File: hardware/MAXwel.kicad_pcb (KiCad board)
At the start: 2 copper layers, 85.1 x 87.2 mm, 155 parts, among them J1 Conn_02x05_Odd_Even, J2 Conn_02x12_Counter_Clockwise, J3 Barrel_Jack_Switch_Pin3Ring, SW1 SW_Push_Dual, SW10 SW_Wuerth_450301014042, SW11 SW_Wuerth_450301014042, SW12 SW_Wuerth_450301014042, SW13 SW_Wuerth_450301014042, SW2 SW_Push_Dual, SW3 SW_Push_Dual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

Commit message: first successfull redesign
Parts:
- moved R1 12.0 mm to (130.6, 58.7)
- moved D1 12.0 mm to (126.5, 58.7)
- moved C1 12.0 mm to (143.3, 47.5), turned to 180 degrees
- moved C2 11.1 mm to (152.3, 48.8), turned to -90 degrees
- moved C5 9.46 mm to (143.3, 46.0), turned to 180 degrees
- moved R31 6.24 mm to (117.9, 94.5), turned to 0 degrees
- moved X2 5.70 mm to (143.3, 51.3), turned to -90 degrees
- moved R45 4.45 mm to (122.2, 63.0), turned to 90 degrees
- moved R50 4.28 mm to (122.2, 33.5), turned to 90 degrees
- moved R42 4.23 mm to (122.2, 77.7), turned to 90 degrees
- moved R48 4.14 mm to (122.2, 48.3), turned to 90 degrees
- moved R49 3.54 mm to (122.2, 44.7), turned to -90 degrees
- moved R43 3.42 mm to (122.2, 74.2), turned to -90 degrees
- moved R51 3.39 mm to (122.2, 30.0), turned to -90 degrees
- moved R33 3.30 mm to (118.1, 84.3), turned to 135 degrees
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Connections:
- C13 pad 1: Net-(C13-Pad1) -> Net-(U5-IO1_4)
- C14 pad 1: Net-(C14-Pad1) -> Net-(U5-IO1_3)
- C3 pad 1: Net-(C3-Pad1) -> Net-(U5-IO1_20)
- C9 pad 1: Net-(C9-Pad1) -> Net-(U5-IO1_19)
- D7 pad 2: unconnected-(D7-A-Pad2) -> Net-(D7-A)
- R1 pad 1: unconnected-(R1-Pad1) -> Net-(U5-IO1_15)
- R2 pad 1: unconnected-(R2-Pad1) -> Net-(U5-IO1_5)
- R3 pad 1: unconnected-(R3-Pad1) -> Net-(U5-IO1_6)
- R4 pad 1: unconnected-(R4-Pad1) -> Net-(U5-IO1_7)
- R42 pad 1: Net-(C3-Pad1) -> Net-(U5-IO1_20)
- R45 pad 1: Net-(C9-Pad1) -> Net-(U5-IO1_19)
- R48 pad 1: Net-(C13-Pad1) -> Net-(U5-IO1_4)
- R5 pad 1: unconnected-(R5-Pad1) -> Net-(U5-IO1_8)
- R50 pad 1: Net-(C14-Pad1) -> Net-(U5-IO1_3)
- R53 pad 2: unconnected-(R53-Pad2) -> Net-(D7-A)
- R62 pad 1: unconnected-(R62-Pad1) -> Net-(U5-IO1_16)
- R63 pad 1: unconnected-(R63-Pad1) -> Net-(U5-IO1_17)
- R65 pad 1: unconnected-(R65-Pad1) -> Net-(U5-IO1_18)
- U5 pad 15: unconnected-(U5-IO1_15-Pad15) -> Net-(U5-IO1_15)
- U5 pad 16: unconnected-(U5-IO1_16-Pad16) -> Net-(U5-IO1_16)
- U5 pad 17: unconnected-(U5-IO1_17-Pad17) -> Net-(U5-IO1_17)
- U5 pad 18: unconnected-(U5-IO1_18-Pad18) -> Net-(U5-IO1_18)
- U5 pad 19: unconnected-(U5-IO1_19-Pad19) -> Net-(U5-IO1_19)
- U5 pad 20: unconnected-(U5-IO1_20-Pad20) -> Net-(U5-IO1_20)
- U5 pad 3: unconnected-(U5-IO1_3-Pad3) -> Net-(U5-IO1_3)
- U5 pad 4: unconnected-(U5-IO1_4-Pad4) -> Net-(U5-IO1_4)
- U5 pad 5: unconnected-(U5-IO1_5-Pad5) -> Net-(U5-IO1_5)
- U5 pad 6: unconnected-(U5-IO1_6-Pad6) -> Net-(U5-IO1_6)
- U5 pad 7: unconnected-(U5-IO1_7-Pad7) -> Net-(U5-IO1_7)
- U5 pad 8: unconnected-(U5-IO1_8-Pad8) -> Net-(U5-IO1_8)
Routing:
- net +3V3: track 0.00 -> 371.0 mm, vias 0 -> 8
- net Net-(J1-Pin_5): track 0.00 -> 82.3 mm
- net Net-(J1-Pin_9): track 0.00 -> 76.5 mm
- net Net-(U5-IO1_3): track 0.00 -> 57.0 mm
- net Net-(J1-Pin_3): track 0.00 -> 55.8 mm
- net Net-(J1-Pin_1): track 0.00 -> 54.7 mm
- net Net-(U5-IO1_4): track 0.00 -> 54.5 mm
- net Net-(U5-IO1_20): track 0.00 -> 48.1 mm
- net Net-(U5-IO1_19): track 0.00 -> 46.8 mm
- net Net-(U5-IO1_8): track 0.00 -> 41.4 mm
- net Net-(U5-IO1_7): track 0.00 -> 39.7 mm
- net Net-(U5-IO1_6): track 0.00 -> 38.0 mm
- net Net-(U5-IO1_5): track 0.00 -> 36.3 mm
- net GND: track 30.1 -> 65.5 mm, vias 0 -> 25
- net Net-(U5-IO1_15): track 0.00 -> 28.3 mm
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- added copper zone on B.Cu, net +3V3

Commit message: squashing pcb layout
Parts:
- moved R77 13.7 mm to (174.2, 70.9), turned to 90 degrees
- moved D17 6.80 mm to (176.3, 74.2), turned to -90 degrees
- moved R13 5.57 mm to (166.9, 78.6), turned to 135 degrees
- moved U6 4.80 mm to (169.5, 71.8)
- moved C24 4.77 mm to (174.2, 74.3)
- moved C8 4.16 mm to (163.7, 73.5)
- moved R42 4.10 mm to (126.2, 77.2), turned to 180 degrees
- moved J1 3.38 mm to (112.4, 87.7)
- moved D2 3.20 mm to (129.7, 49.9)
- moved D3 3.20 mm to (129.7, 52.2)
- moved R1 3.20 mm to (133.7, 59.1)
- moved R2 3.20 mm to (133.8, 49.9)
- moved R3 3.20 mm to (133.8, 52.2)
- moved R4 3.20 mm to (133.8, 54.5)
- moved R5 3.20 mm to (133.8, 56.8)
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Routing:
- net GND: track 65.5 -> 83.5 mm, vias 25 -> 313
- net +3V3: track 371.0 -> 362.4 mm
- net Net-(U5-IO1_20): track 48.1 -> 41.0 mm
- net Net-(U1-E): track 7.61 -> 13.4 mm
- net +5V: track 21.6 -> 27.3 mm
- net Net-(U5-IO2_62/GCLK2): track 18.5 -> 13.0 mm
- net Net-(U5-IO1_18): track 26.6 -> 21.9 mm
- net Net-(U5-IO1_4): track 54.5 -> 49.8 mm
- net Net-(U5-IO1_17): track 27.4 -> 23.1 mm
- net Net-(U5-IO1_16): track 28.0 -> 23.7 mm
- net Net-(U5-IO1_15): track 28.3 -> 24.0 mm
- net Net-(J1-Pin_9): track 76.5 -> 72.5 mm
- net Net-(J1-Pin_5): track 82.3 -> 78.5 mm
- net Net-(J1-Pin_1): track 54.7 -> 51.0 mm
- net Net-(U5-IO1_19): track 46.8 -> 43.8 mm
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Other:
- board size 85.1 x 87.2 mm -> 78.7 x 85.7 mm

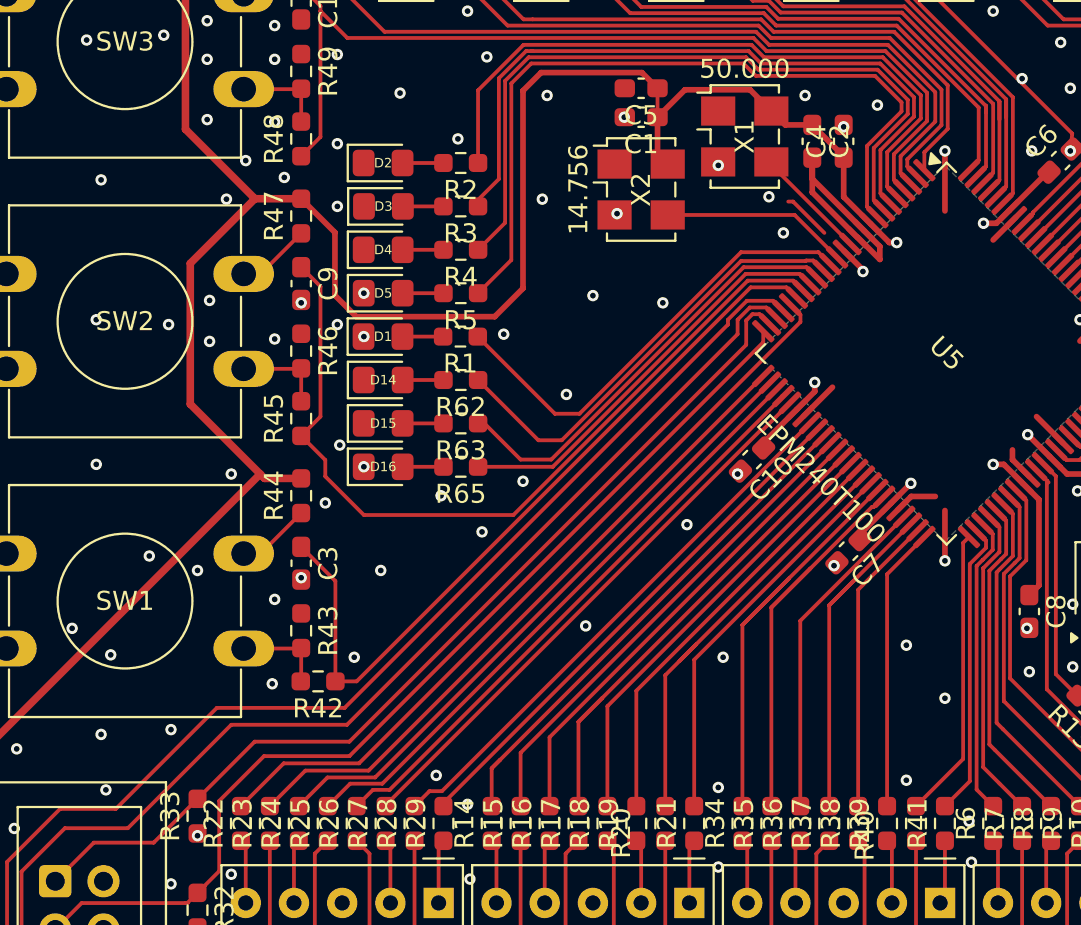
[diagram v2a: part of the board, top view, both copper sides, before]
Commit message: JTAG interface: increase spacing, add more GND for better EMI
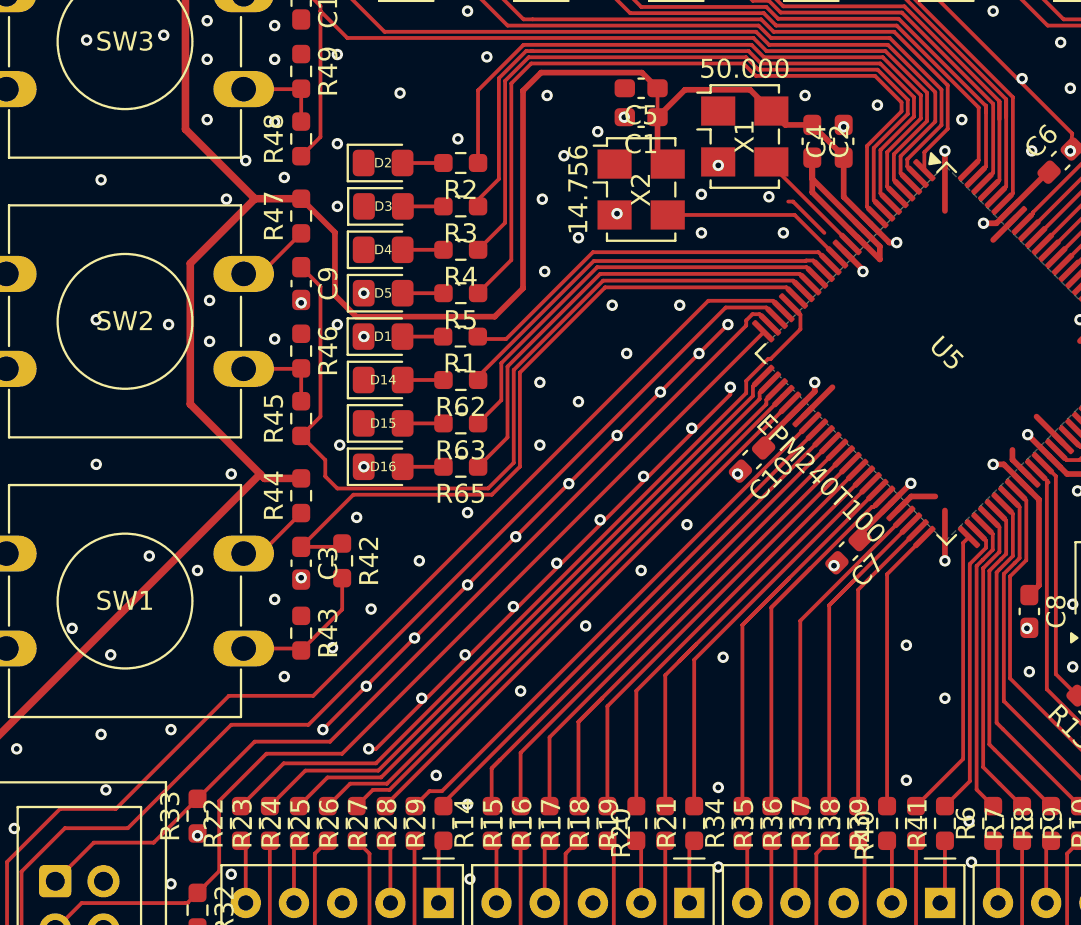
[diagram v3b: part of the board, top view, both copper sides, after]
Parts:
- moved R42 6.48 mm to (127.5, 70.9), turned to -90 degrees
- moved R43 0.13 mm to (125.3, 74.7)
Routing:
- net GND: track 83.5 -> 141.9 mm, vias 313 -> 342
- net Net-(U5-IO1_20): track 41.0 -> 37.1 mm
- net Net-(U5-IO1_15): track 24.0 -> 20.8 mm
- net Net-(R42-Pad2): track 4.77 -> 7.74 mm
- net Net-(U5-IO1_16): track 23.7 -> 21.1 mm
- net Net-(U5-IO1_18): track 21.9 -> 24.1 mm
- net Net-(U5-IO1_19): track 43.8 -> 45.5 mm
- net Net-(U5-IO1_21): track 41.2 -> 41.8 mm
- net Net-(J1-Pin_1): track 51.0 -> 50.4 mm

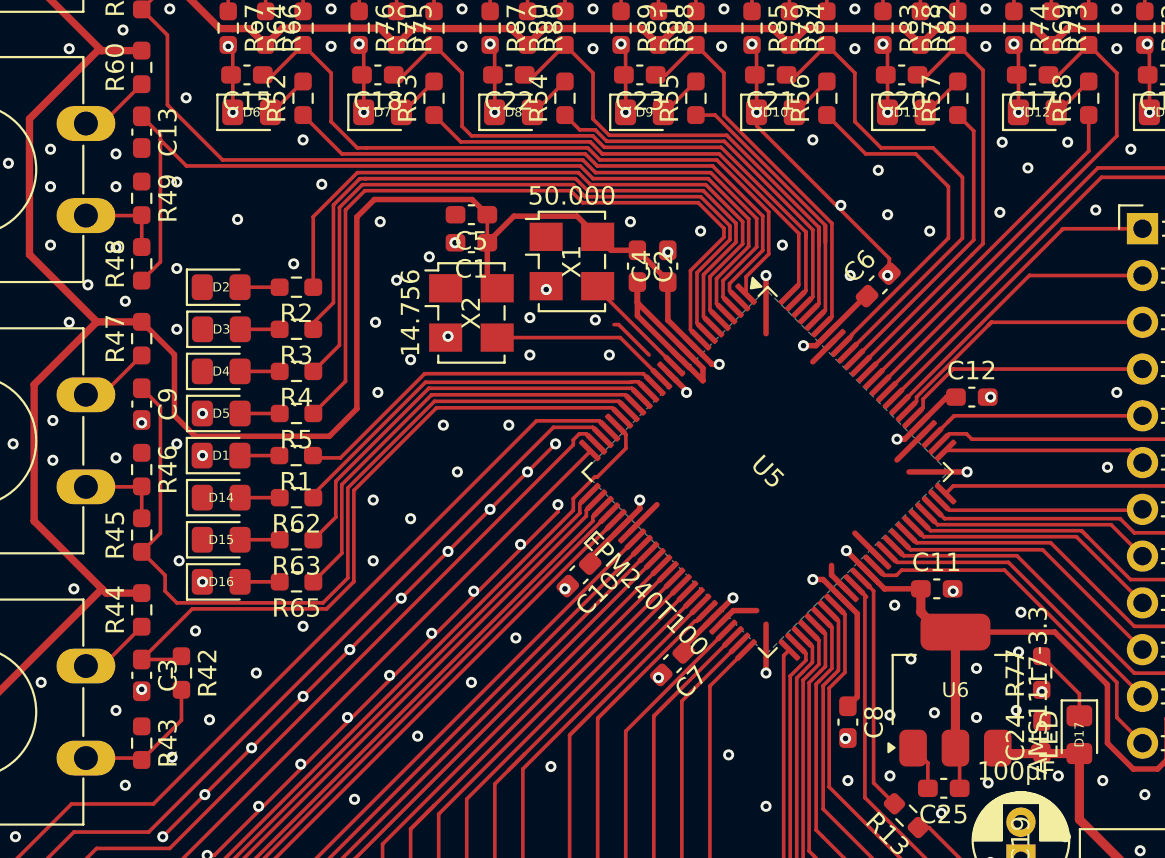
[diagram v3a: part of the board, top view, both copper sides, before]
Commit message: optimized traces
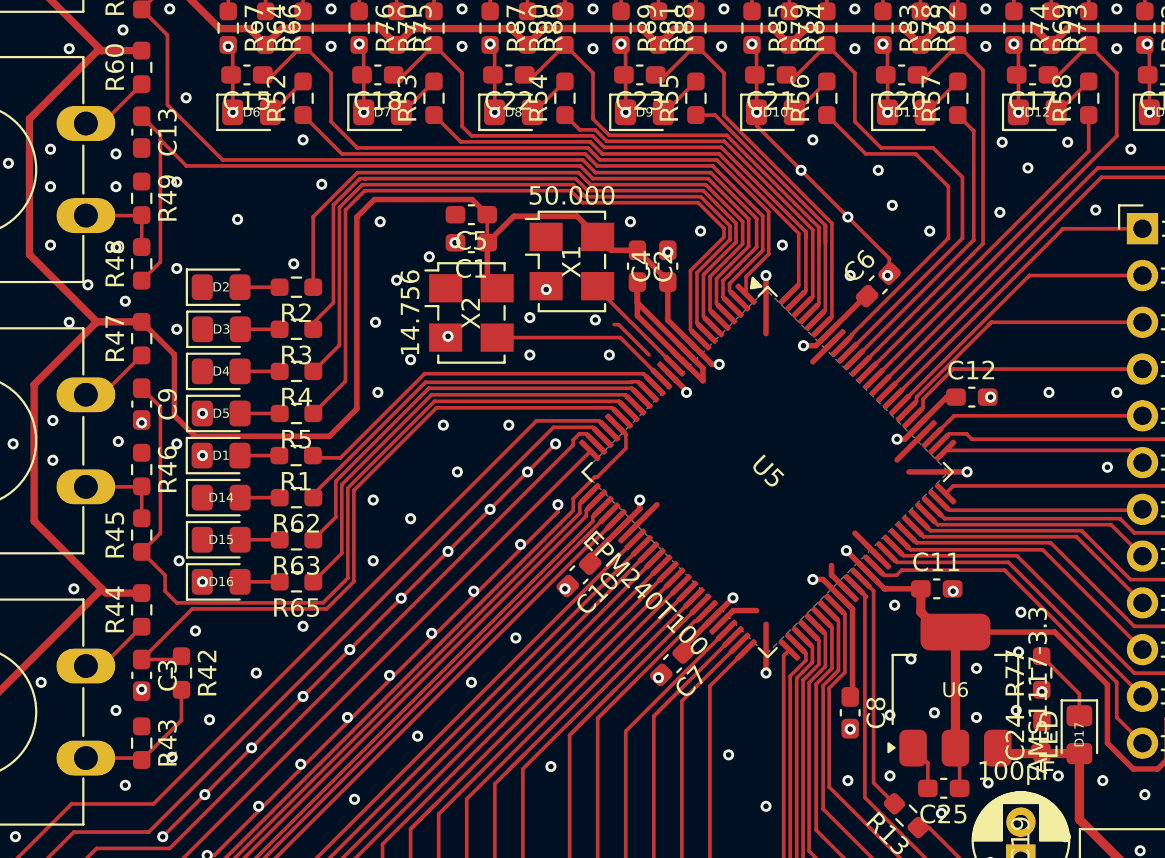
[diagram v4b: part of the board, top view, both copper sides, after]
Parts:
- moved C8 0.52 mm to (163.8, 73.0)
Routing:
- net +3V3: track 362.4 -> 361.8 mm
- net GND: track 141.9 -> 141.7 mm, vias 342 -> 344
